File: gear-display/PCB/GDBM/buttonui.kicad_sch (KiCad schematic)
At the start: 3 parts

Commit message: updates
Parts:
- removed J?: Con_Screw_1x04_691313510004, KD_Connector_Screw:CON_508_1X04_691313510004_Mated, symbol KD_Connector_Screw:Con_Screw_1x04_691313510004
- removed R?: R_0402_4700_1%, KD_Resistor:R_0402_1005Metric, symbol KD_Resistor:R_0402_4700_1%
- added C?: C_0805_1u_X7R_25V, KD_Capacitor:C_0805_2012Metric, symbol KD_Capacitor:C_0805_1u_X7R_25V
- added M?: Knob_6mm_BL_RED_CLIFF_CL170842CR, KD_Mechanical:Knob_CLIFF_CL170842CR, symbol KD_Mechanical:Knob_6mm_BL_RED_CLIFF_CL170842CR
- added R?: R_0402_4700_1%, KD_Resistor:R_0402_1005Metric, symbol KD_Resistor:R_0402_4700_1%
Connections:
- net +3V3: now also R?.1
- net GND: now also C?.2
- net POT_W: now also C?.1, R?.2; no longer R?.2
- new net: R?.1, R?.2

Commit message: rikki
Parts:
- R29: renamed from R?; footprint KD_Resistor:R_0402_1005Metric -> KD_Resistor:RESC1005X40N
- gave numbers to parts that had none: 3
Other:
- company: (none) -> Kallio Designs Oy
- title: (none) -> Gear Display Board
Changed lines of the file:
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@@
 (kicad_sch (version 20211123) (generator eeschema)
   (paper "A4")
+  (title_block
+    (title "Gear Display Board")
+    (date "2022-08-13")
+    (rev "1.0")
+    (company "Kallio Designs Oy")
+    (comment 1 "Teemu Latonen")
+    (comment 2 "000064")
+    (comment 3 "000065")
+  )
   (junction (at 127 134.62) (diameter 0) (color 0 0 0 0)
   )
@@
   (symbol (lib_id "power:+3.3V") (at 105.41 121.92 0) (unit 1)
     (in_bom yes) (on_board yes) (fields_autoplaced)
-    (property "Reference" "#PWR?" (id 0) (at 105.41 125.73 0)
+    (property "Reference" "#PWR0134" (id 0) (at 105.41 125.73 0)
       (effects (font (size 1.27 1.27)) hide)
     )
@@
   (symbol (lib_id "KD_Resistor:Pot_V_10k_CUI_PT01-D120K2-B103") (at 105.41 134.62 0) (unit 1)
     (in_bom yes) (on_board yes) (fields_autoplaced)
-    (property "Reference" "R?" (id 0) (at 102.87 133.3499 0)
+    (property "Reference" "R28" (id 0) (at 102.87 133.3499 0)
       (effects (font (size 1.27 1.27)) (justify right))
     )
@@
   (symbol (lib_id "KD_Mechanical:Knob_6mm_BL_RED_CLIFF_CL170842CR") (at 73.66 119.38 0) (unit 1)
     (in_bom yes) (on_board yes) (fields_autoplaced)
-    (property "Reference" "M?" (id 0) (at 80.01 116.5224 0)
+    (property "Reference" "M1" (id 0) (at 80.01 116.5224 0)
       (effects (font (size 1.27 1.27)) (justify left))
     )
@@
   (symbol (lib_id "power:GND") (at 105.41 147.32 0) (unit 1)
     (in_bom yes) (on_board yes)
-    (property "Reference" "#PWR?" (id 0) (at 105.41 153.67 0)
+    (property "Reference" "#PWR0132" (id 0) (at 105.41 153.67 0)
       (effects (font (size 1.27 1.27)) hide)
     )
@@
   (symbol (lib_id "power:GND") (at 127 147.32 0) (unit 1)
     (in_bom yes) (on_board yes)
-    (property "Reference" "#PWR?" (id 0) (at 127 153.67 0)
+    (property "Reference" "#PWR0133" (id 0) (at 127 153.67 0)
       (effects (font (size 1.27 1.27)) hide)
     )
@@
   (symbol (lib_id "KD_Resistor:R_0402_4700_1%") (at 120.65 134.62 90) (unit 1)
     (in_bom yes) (on_board yes) (fields_autoplaced)
-    (property "Reference" "R?" (id 0) (at 120.65 128.27 90))
+    (property "Reference" "R29" (id 0) (at 120.65 128.27 90))
     (property "Value" "R_0402_4700_1%" (id 1) (at 88.9 147.32 0)
       (effects (font (size 1.27 1.27)) (justify left) hide)
     )
-    (property "Footprint" "KD_Resistor:R_0402_1005Metric" (id 2) (at 106.68 147.32 0)
+    (property "Footprint" "KD_Resistor:RESC1005X40N" (id 2) (at 106.68 147.32 0)
       (effects (font (size 1.27 1.27)) (justify left) hide)
     )
@@
   (symbol (lib_id "KD_Capacitor:C_0805_1u_X7R_25V") (at 127 140.97 0) (unit 1)
     (in_bom yes) (on_board yes)
-    (property "Reference" "C?" (id 0) (at 129.54 139.7 0)
+    (property "Reference" "C21" (id 0) (at 129.54 139.7 0)
       (effects (font (size 1.27 1.27)) (justify left))
     )

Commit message: PSU and LED powering changed
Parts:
- C21: footprint KD_Capacitor:C_0805_2012Metric -> KD_Capacitor:CAPC2012X135N
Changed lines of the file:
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@@
       (effects (font (size 1.27 1.27)) (justify left) hide)
     )
-    (property "Footprint" "KD_Capacitor:C_0805_2012Metric" (id 2) (at 114.3 127 0)
+    (property "Footprint" "KD_Capacitor:CAPC2012X135N" (id 2) (at 114.3 127 0)
       (effects (font (size 1.27 1.27)) (justify left) hide)
     )

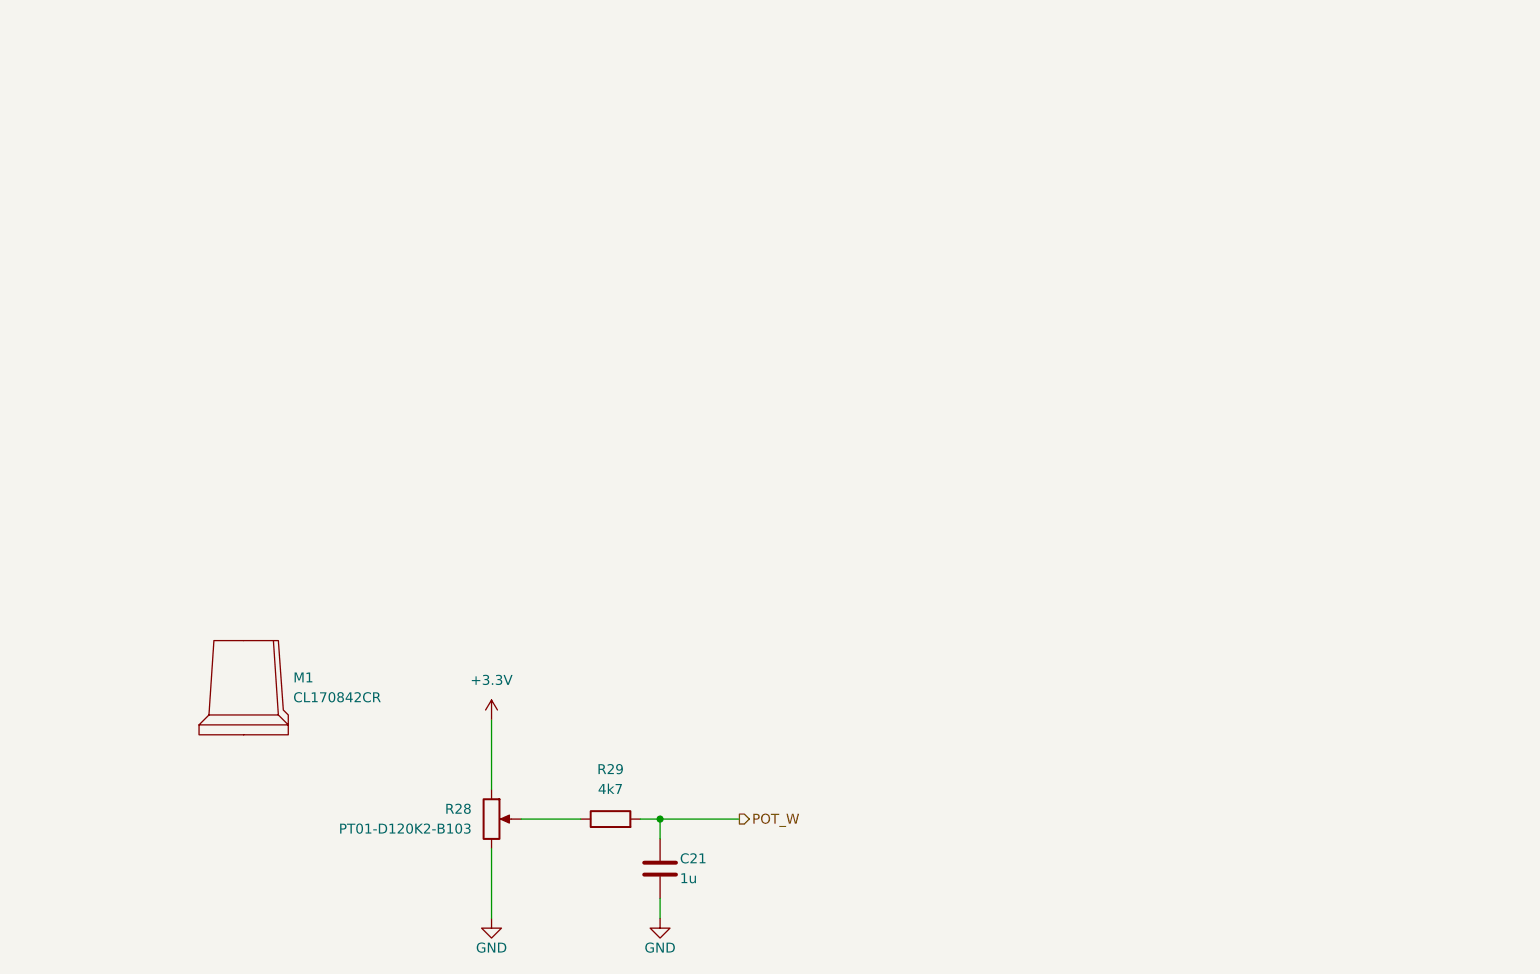
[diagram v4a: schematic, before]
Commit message: bugfixes
added 555 circuit for brightness control
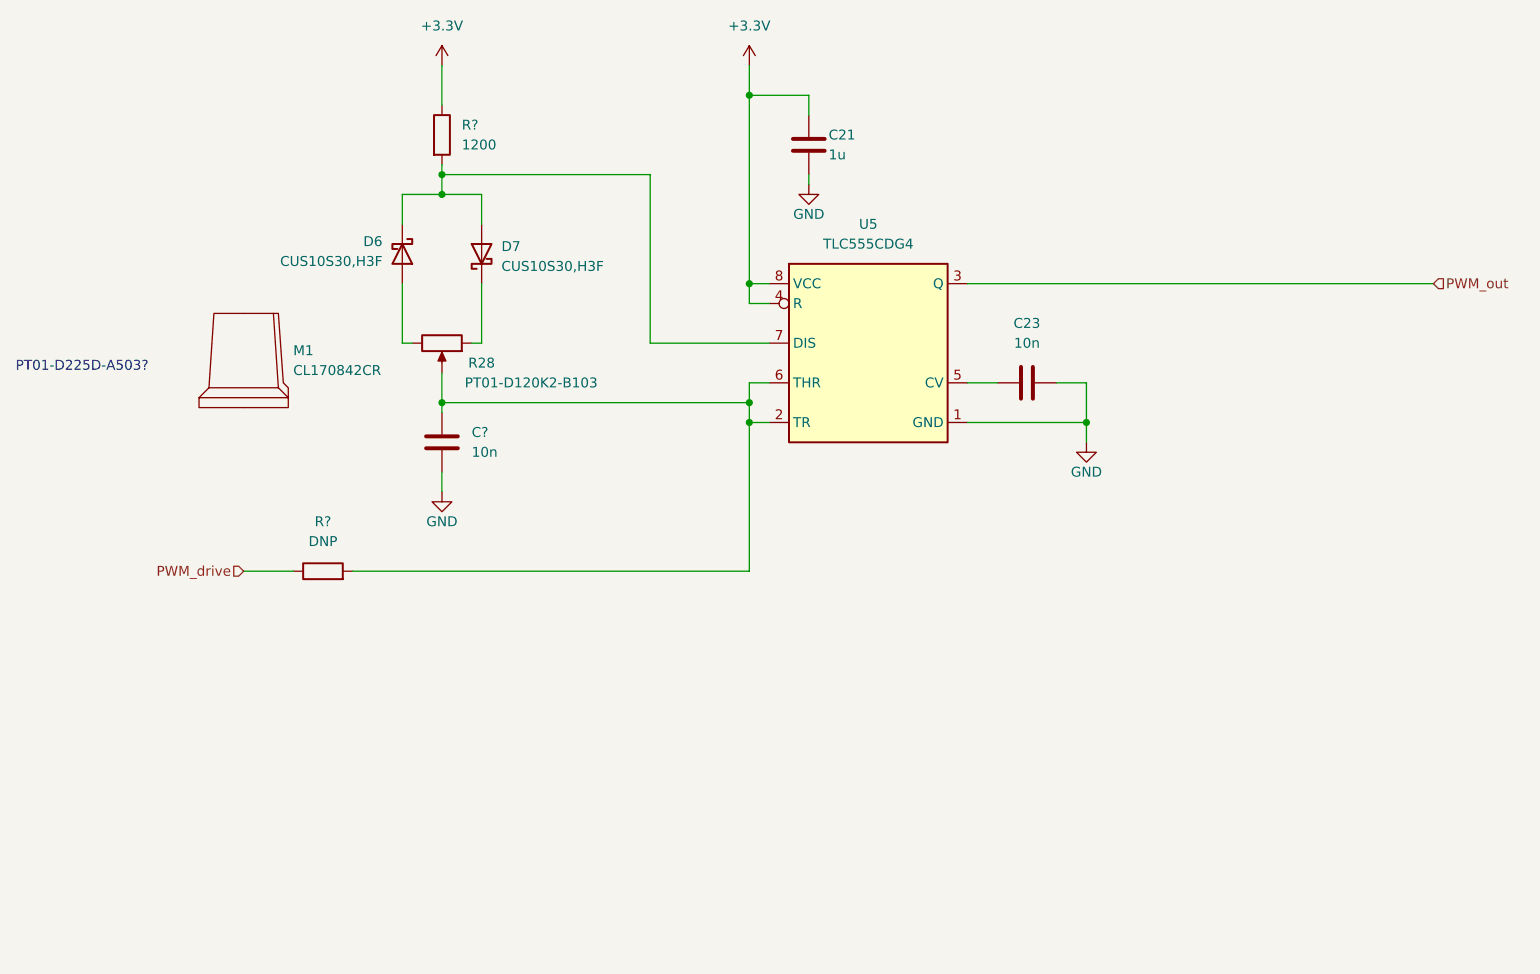
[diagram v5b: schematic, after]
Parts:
- removed R29: R_0402_4700_1%, KD_Resistor:RESC1005X40N, symbol KD_Resistor:R_0402_4700_1%
- added C23, C?: C_0603_10n_X7R_100V, KD_Capacitor:CAPC1608X90N, symbol KD_Capacitor:C_0603_10n_X7R_100V
- added D6, D7: Schottky_30V_1A_Toshiba_CUS10S30, KD_Diode:D_SOD-323, symbol KD_Diode:Schottky_30V_1A_Toshiba_CUS10S30
- added R?: R_0805_1200_5%, KD_Resistor:RESC2012X60N, symbol KD_Resistor:R_0805_1200_5%
- added R?: R_0603_DNP, KD_Resistor:RESC1608X55N_DNP, symbol KD_Resistor:R_0603_DNP
- added U5: Timer_Oscillator_TLC555CDG4, KD_Package_SO:SOIC127P600X175-8, symbol KD_IC_Other:Timer_Oscillator_TLC555CDG4
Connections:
- net POT_W is gone; now on net +3V3: C21.1
- net +3V3: now also R?.1, U5.4 (R), U5.8 (VCC); no longer R28.1
- net GND: now also C23.2, C?.1, U5.1 (GND); no longer R28.3
- net at R28.2: now also C?.2, R?.2, U5.2 (TR), U5.6 (THR)
- new net: D6.1 (K), D7.2 (A), R?.2, U5.7 (DIS)
- new net: D7.1 (K), R28.1
- new net: D6.2 (A), R28.3
- new net: C23.1, U5.5 (CV)
- new net PWM_drive: R?.1
- new net PWM_out: U5.3 (Q)
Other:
- note added: "PT01-D225D-A503?"
- moved on the sheet: C21, M1, R28

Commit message: layout
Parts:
- R28: symbol KD_Resistor:Pot_V_10k_CUI_PT01-D120K2-B103 -> KD_Resistor:Pot_V_50k_CUI_PT01-D225D-A503; Code PT01-D120K2-B103 -> 50k; MFG_PartNo PT01-D120K2-B103 -> PT01-D225D-A503; Supplier_PartNo 2223-PT01-D120K2-B103-ND -> 2223-PT01-D225D-A503-ND
- gave numbers to parts that had none: 3
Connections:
- net +3V3 renamed +5V
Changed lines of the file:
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@@
   (title_block
     (title "Gear Display Board")
-    (date "2022-08-13")
-    (rev "1.0")
+    (date "2023-01-05")
+    (rev "2.0")
     (company "Kallio Designs Oy")
     (comment 1 "Teemu Latonen")
@@
   (symbol (lib_id "KD_Capacitor:C_0603_10n_X7R_100V") (at 99.06 86.36 180) (unit 1)
     (in_bom yes) (on_board yes) (fields_autoplaced)
-    (property "Reference" "C?" (id 0) (at 102.87 85.0899 0)
+    (property "Reference" "C24" (id 0) (at 102.87 85.0899 0)
       (effects (font (size 1.27 1.27)) (justify right))
     )
@@
   (symbol (lib_id "power:GND") (at 146.05 53.34 0) (unit 1)
     (in_bom yes) (on_board yes)
-    (property "Reference" "#PWR?" (id 0) (at 146.05 59.69 0)
+    (property "Reference" "#PWR04" (id 0) (at 146.05 59.69 0)
       (effects (font (size 1.27 1.27)) hide)
     )
@@
   (symbol (lib_id "KD_Resistor:R_0805_1200_5%") (at 99.06 46.99 0) (unit 1)
     (in_bom yes) (on_board yes) (fields_autoplaced)
-    (property "Reference" "R?" (id 0) (at 101.6 45.7199 0)
+    (property "Reference" "R33" (id 0) (at 101.6 45.7199 0)
       (effects (font (size 1.27 1.27)) (justify left))
     )
@@
     (pin "2")
   )
-  (symbol (lib_id "KD_Resistor:Pot_V_10k_CUI_PT01-D120K2-B103") (at 99.06 73.66 270) (unit 1)
-    (in_bom yes) (on_board yes)
-    (property "Reference" "R28" (id 0) (at 104.14 76.2 90))
+  (symbol (lib_id "KD_Resistor:Pot_V_50k_CUI_PT01-D225D-A503") (at 99.06 73.66 270) (unit 1)
+    (in_bom yes) (on_board yes) (fields_autoplaced)
+    (property "Reference" "R28" (id 0) (at 99.06 67.31 90))
     (property "Value" "Pot_V_10k_CUI_PT01-D120K2-B103" (id 1) (at 130.81 60.96 0)
       (effects (font (size 1.27 1.27)) (justify left) hide)
@@
       (effects (font (size 1.27 1.27)) (justify left) hide)
     )
-    (property "Datasheet" "" (id 3) (at 110.49 60.96 0)
-      (effects (font (size 1.27 1.27)) (justify left) hide)
-    )
-    (property "Code" "PT01-D120K2-B103" (id 4) (at 110.49 78.74 90))
+    (property "Datasheet" "https://www.cuidevices.com/product/resource/pt01.pdf" (id 3) (at 110.49 60.96 0)
+      (effects (font (size 1.27 1.27)) (justify left) hide)
+    )
+    (property "Code" "50k" (id 4) (at 99.06 69.85 90))
     (property "Manufacturer" "CUI Devices" (id 5) (at 128.27 60.96 0)
       (effects (font (size 1.27 1.27)) (justify left) hide)
     )
-    (property "MFG_PartNo" "PT01-D120K2-B103" (id 6) (at 125.73 60.96 0)
+    (property "MFG_PartNo" "PT01-D225D-A503" (id 6) (at 125.73 60.96 0)
       (effects (font (size 1.27 1.27)) (justify left) hide)
     )
@@
       (effects (font (size 1.27 1.27)) (justify left) hide)
     )
-    (property "Supplier_PartNo" "2223-PT01-D120K2-B103-ND" (id 8) (at 120.65 60.96 0)
+    (property "Supplier_PartNo" "2223-PT01-D225D-A503-ND" (id 8) (at 120.65 60.96 0)
       (effects (font (size 1.27 1.27)) (justify left) hide)
     )
@@
     (pin "2")
   )
+  (symbol (lib_id "power:+5V") (at 138.43 38.1 0) (unit 1)
+    (in_bom yes) (on_board yes) (fields_autoplaced)
+    (property "Reference" "#PWR0133" (id 0) (at 138.43 41.91 0)
+      (effects (font (size 1.27 1.27)) hide)
+    )
+    (property "Value" "+5V" (id 1) (at 138.43 33.02 0))
+    (property "Footprint" "" (id 2) (at 138.43 38.1 0)
+      (effects (font (size 1.27 1.27)) hide)
+    )
+    (property "Datasheet" "" (id 3) (at 138.43 38.1 0)
+      (effects (font (size 1.27 1.27)) hide)
+    )
+    (pin "1")
+  )
   (symbol (lib_id "KD_Resistor:R_0603_DNP") (at 83.82 102.87 90) (unit 1)
     (in_bom yes) (on_board yes) (fields_autoplaced)
-    (property "Reference" "R?" (id 0) (at 83.82 96.52 90))
+    (property "Reference" "R29" (id 0) (at 83.82 96.52 90))
     (property "Value" "R_0603_DNP" (id 1) (at 52.07 115.57 0)
       (effects (font (size 1.27 1.27)) (justify left) hide)
@@
   (symbol (lib_id "power:GND") (at 99.06 92.71 0) (unit 1)
     (in_bom yes) (on_board yes)
-    (property "Reference" "#PWR?" (id 0) (at 99.06 99.06 0)
+    (property "Reference" "#PWR02" (id 0) (at 99.06 99.06 0)
       (effects (font (size 1.27 1.27)) hide)
     )
@@
     (pin "2")
   )
-  (symbol (lib_id "power:+3.3V") (at 99.06 38.1 0) (unit 1)
-    (in_bom yes) (on_board yes) (fields_autoplaced)
-    (property "Reference" "#PWR?" (id 0) (at 99.06 41.91 0)
-      (effects (font (size 1.27 1.27)) hide)
-    )
-    (property "Value" "+3.3V" (id 1) (at 99.06 33.02 0))
-    (property "Footprint" "" (id 2) (at 99.06 38.1 0)
-      (effects (font (size 1.27 1.27)) hide)
-    )
-    (property "Datasheet" "" (id 3) (at 99.06 38.1 0)
-      (effects (font (size 1.27 1.27)) hide)
-    )
-    (pin "1")
-  )
   (symbol (lib_id "KD_Capacitor:C_0805_1u_X7R_25V") (at 146.05 48.26 0) (unit 1)
     (in_bom yes) (on_board yes)
@@
     (pin "2")
   )
-  (symbol (lib_id "power:+3.3V") (at 138.43 38.1 0) (unit 1)
-    (in_bom yes) (on_board yes) (fields_autoplaced)
-    (property "Reference" "#PWR?" (id 0) (at 138.43 41.91 0)
-      (effects (font (size 1.27 1.27)) hide)
-    )
-    (property "Value" "+3.3V" (id 1) (at 138.43 33.02 0))
-    (property "Footprint" "" (id 2) (at 138.43 38.1 0)
-      (effects (font (size 1.27 1.27)) hide)
-    )
-    (property "Datasheet" "" (id 3) (at 138.43 38.1 0)
-      (effects (font (size 1.27 1.27)) hide)
-    )
+  (symbol (lib_id "power:+5V") (at 99.06 38.1 0) (unit 1)
+    (in_bom yes) (on_board yes) (fields_autoplaced)
+    (property "Reference" "#PWR0132" (id 0) (at 99.06 41.91 0)
+      (effects (font (size 1.27 1.27)) hide)
+    )
+    (property "Value" "+5V" (id 1) (at 99.06 33.02 0))
+    (property "Footprint" "" (id 2) (at 99.06 38.1 0)
+      (effects (font (size 1.27 1.27)) hide)
+    )
+    (property "Datasheet" "" (id 3) (at 99.06 38.1 0)
+      (effects (font (size 1.27 1.27)) hide)
+    )
